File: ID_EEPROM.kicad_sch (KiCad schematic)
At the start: 2 parts, among them U2 M24C64

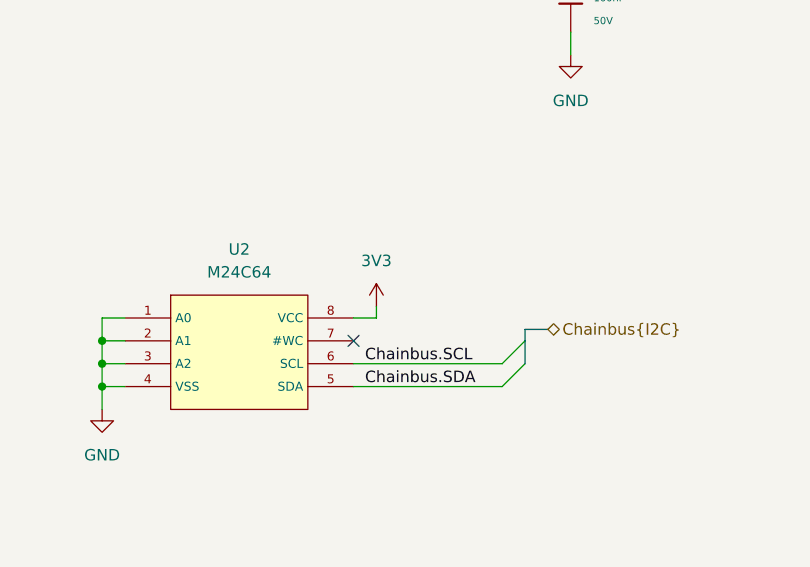
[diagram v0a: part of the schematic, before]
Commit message: Added mechanical standard and updated readme
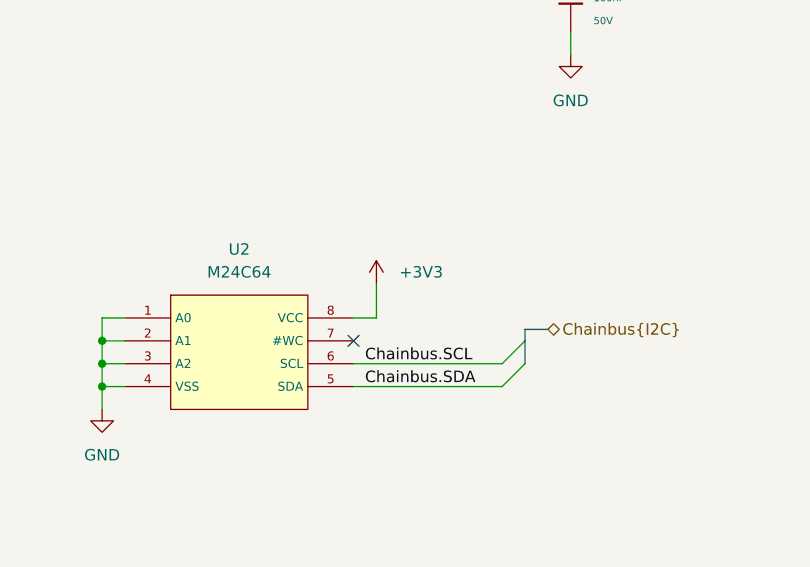
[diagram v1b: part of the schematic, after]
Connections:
- net 3V3 is gone; now on net +3V3: U2.8 (VCC)
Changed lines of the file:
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@@
 	(wire
 		(pts
-			(xy 154.94 95.25) (xy 154.94 96.52)
+			(xy 154.94 92.71) (xy 154.94 96.52)
 		)
 		(stroke
@@
 			)
 		)
+		(property "Sim.Device" ""
+			(at 139.7 101.6 0)
+			(effects
+				(font
+					(size 1.27 1.27)
+				)
+				(hide yes)
+			)
+		)
 		(pin "3"
 		)
@@
 	)
 	(symbol
-		(lib_id "power:+3.3V")
-		(at 154.94 95.25 0)
-		(unit 1)
-		(exclude_from_sim no)
-		(in_bom yes)
-		(on_board yes)
-		(dnp no)
-		(fields_autoplaced yes)
-		(property "Reference" "#PWR043"
-			(at 154.94 99.06 0)
-			(effects
-				(font
-					(size 1.27 1.27)
-				)
-				(hide yes)
-			)
-		)
-		(property "Value" "3V3"
-			(at 154.94 90.17 0)
-			(effects
-				(font
-					(size 1.27 1.27)
-				)
-			)
-		)
-		(property "Footprint" ""
-			(at 154.94 95.25 0)
-			(effects
-				(font
-					(size 1.27 1.27)
-				)
-				(hide yes)
-			)
-		)
-		(property "Datasheet" ""
-			(at 154.94 95.25 0)
-			(effects
-				(font
-					(size 1.27 1.27)
-				)
-				(hide yes)
-			)
-		)
-		(property "Description" "Power symbol creates a global label with name \"+3.3V\""
-			(at 154.94 95.25 0)
-			(effects
-				(font
-					(size 1.27 1.27)
-				)
-				(hide yes)
-			)
-		)
-		(pin "1"
-		)
-		(instances
-			(project "MMS2_hat_template_small"
-				(path "/6596548a-44e0-46d8-8624-fd71cf4a3e17/56050d79-5900-47d6-893d-3da0e8bf5810"
-					(reference "#PWR043")
-					(unit 1)
-				)
-			)
-		)
-	)
-	(symbol
 		(lib_id "PCM_JLCPCB-Capacitors:0603,100nF")
 		(at 176.53 60.96 0)
@@
 			)
 		)
+		(property "Sim.Device" ""
+			(at 176.53 60.96 0)
+			(effects
+				(font
+					(size 1.27 1.27)
+				)
+				(hide yes)
+			)
+		)
 		(pin "1"
 		)
@@
 					(unit 1)
 				)
+			)
+		)
+	)
+	(symbol
+		(lib_id "power:+5V")
+		(at 154.94 92.71 0)
+		(mirror y)
+		(unit 1)
+		(exclude_from_sim no)
+		(in_bom yes)
+		(on_board yes)
+		(dnp no)
+		(fields_autoplaced yes)
+		(property "Reference" "#PWR043"
+			(at 154.94 96.52 0)
+			(effects
+				(font
+					(size 1.27 1.27)
+				)
+				(hide yes)
+			)
+		)
+		(property "Value" "+3V3"
+			(at 157.48 91.4399 0)
+			(effects
+				(font
+					(size 1.27 1.27)
+				)
+				(justify right)
+			)
+		)
+		(property "Footprint" ""
+			(at 154.94 92.71 0)
+			(effects
+				(font
+					(size 1.27 1.27)
+				)
+				(hide yes)
+			)
+		)
+		(property "Datasheet" ""
+			(at 154.94 92.71 0)
+			(effects
+				(font
+					(size 1.27 1.27)
+				)
+				(hide yes)
+			)
+		)
+		(property "Description" "Power symbol creates a global label with name \"+5V\""
+			(at 154.94 92.71 0)
+			(effects
+				(font
+					(size 1.27 1.27)
+				)
+				(hide yes)
+			)
+		)
+		(pin "1"
+		)
+		(instances
+			(project "MMS3_hat_stepper_controler"
+				(path "/6596548a-44e0-46d8-8624-fd71cf4a3e17/56050d79-5900-47d6-893d-3da0e8bf5810"
+					(reference "#PWR043")
+					(unit 1)
+				)
